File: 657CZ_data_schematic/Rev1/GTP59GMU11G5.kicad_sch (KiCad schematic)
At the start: 2 parts, among them J10 DE9_Socket, J13 DE9_Socket

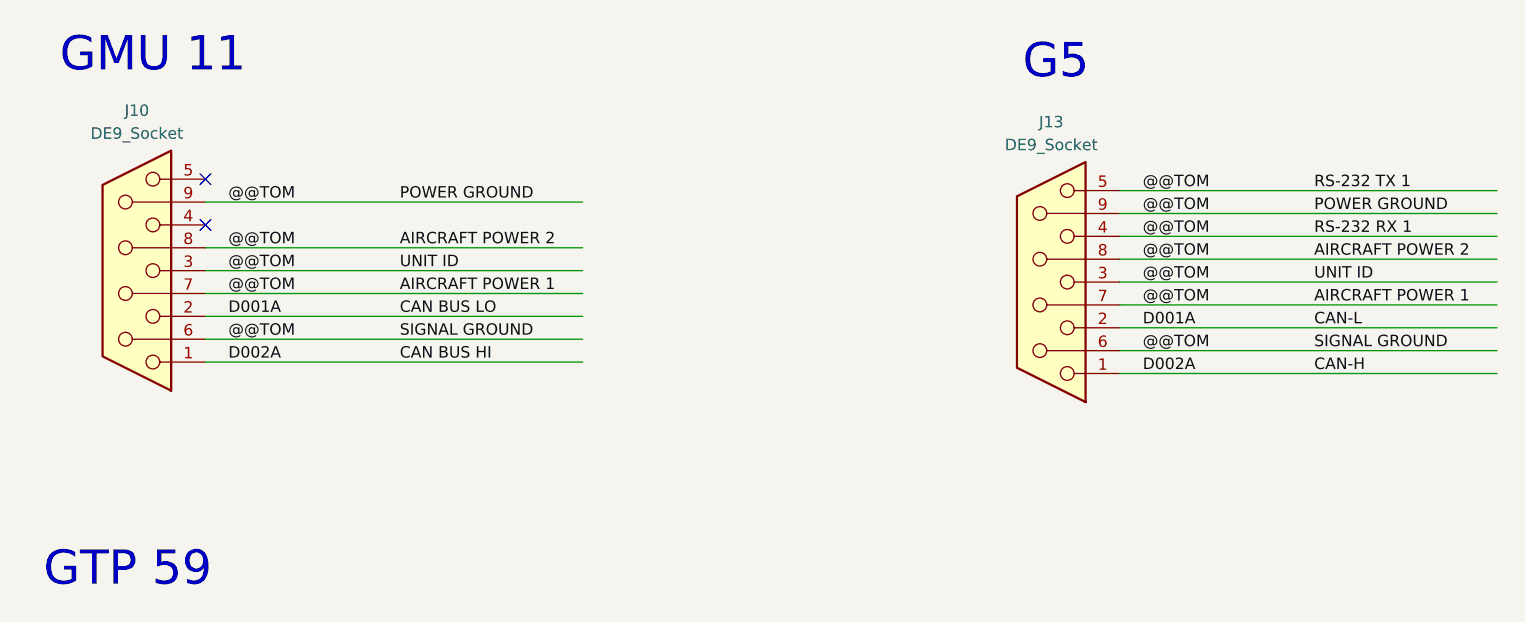
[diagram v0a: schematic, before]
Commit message: added data connections after AvClassics wiring. completed LRUs GMU, GDU, GSU, GAD, GNC, GTX, GTR  Not completed GMA, GEA and autopilot LRUs
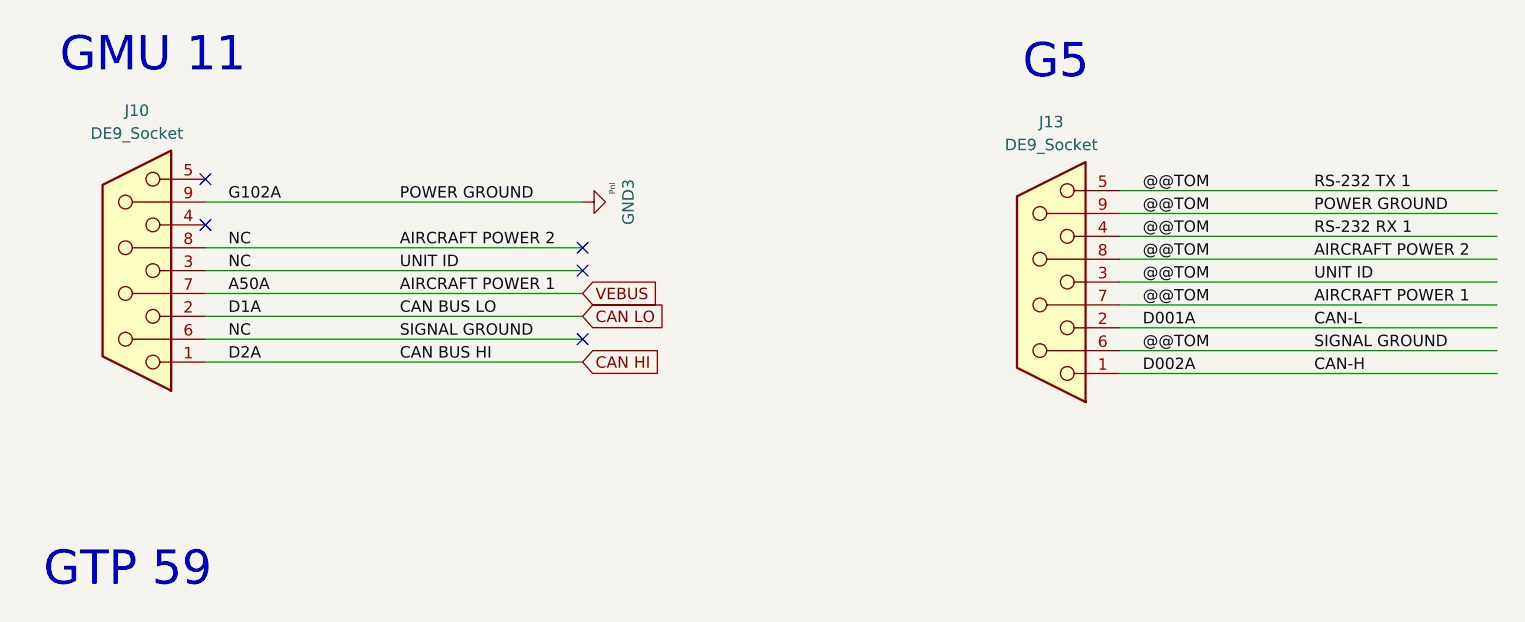
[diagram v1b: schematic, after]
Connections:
- net @@TOM renamed GND3
- net CAN BUS HI renamed CAN HI
- net CAN HI: no longer J13.1
- net CAN BUS LO renamed CAN LO
- net CAN LO: no longer J13.2
- new net CAN-H: J13.1
- new net CAN-L: J13.2
- no-connect marks 2 -> 5
